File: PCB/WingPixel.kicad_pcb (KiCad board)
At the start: 2 copper layers, 50.8 x 22.9 mm, 21 parts, among them J1 Barrel_Jack, J2 Screw_Terminal_01x04, J3 Conn_01x16, J4 Conn_01x12, J5 TriSolderJumper, J6 Conn_01x02, SW1 SW_Push, U1 WingPixel, U2 LSF0102DCUR

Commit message: Final PCB cleanup, fixed LvlShft wiring.
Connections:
- U2 pad 7: VLED -> Net-(C3-Pad2)
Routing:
- net VLED: track 33.1 -> 28.7 mm
- net Net-(C3-Pad2): track 4.43 -> 4.93 mm
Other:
- board text added: "CLK"
- board text added: "DATA"
- board text added: "GND"
- board text added: "Power Feather From EXT"
- board text added: "VLED"
- board text removed: "EXT >USB"
- board text removed: "LED"

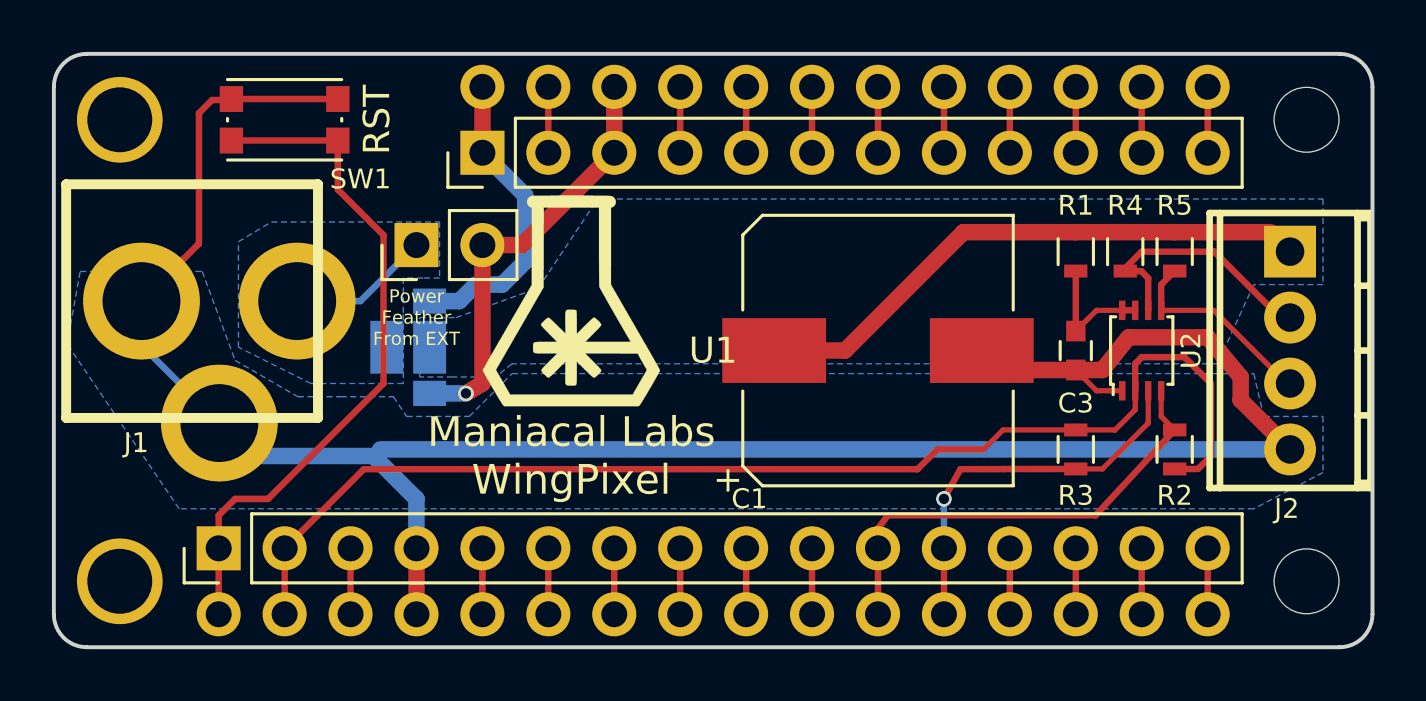
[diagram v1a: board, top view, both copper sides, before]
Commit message: Added placeholders for cuttable traces
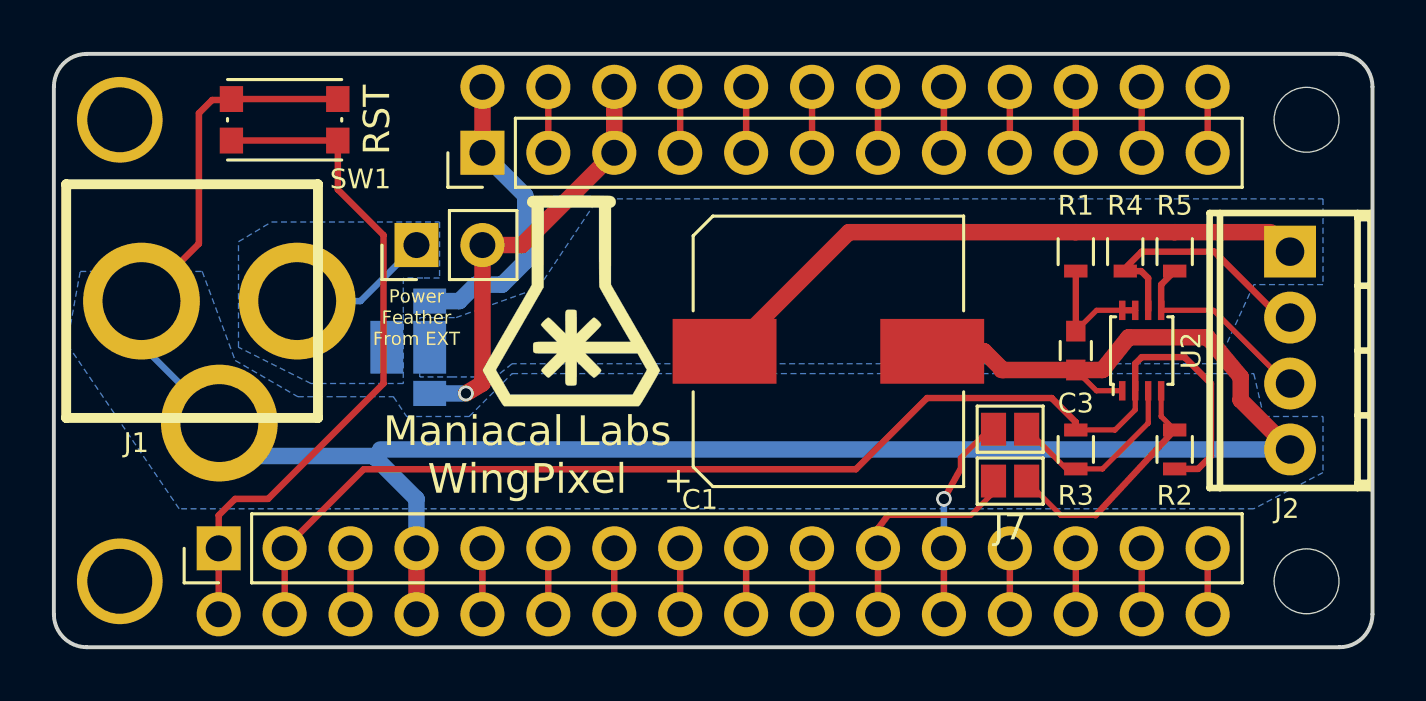
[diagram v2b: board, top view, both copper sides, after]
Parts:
- added J7: GS2, Connectors:GS2, F.Cu at (72.4, 44.4)
- added J8: GS2, Connectors:GS2, F.Cu at (72.4, 42.4)
- moved C1 1.91 mm to (65.4, 39.4)
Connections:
- J3 pad 11: SCLK -> Net-(J3-Pad11)
- J3 pad 12: MOSI -> Net-(J3-Pad12)
- U1 pad 11: SCLK -> Net-(J3-Pad11)
- U1 pad 12: MOSI -> Net-(J3-Pad12)
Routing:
- net Net-(J3-Pad11): track 0.00 -> 8.81 mm
- net SCLK: track 18.2 -> 9.42 mm
- net Net-(J3-Pad12): track 0.00 -> 7.92 mm, vias 0 -> 1
- net MOSI: track 15.0 -> 7.29 mm, vias 1 -> 0
- net GND: track 85.6 -> 87.6 mm
- net VLED: track 28.7 -> 30.7 mm
- net V3v3: track 47.4 -> 48.9 mm

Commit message: Rotated Cap
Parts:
- turned C1 to 270 degrees
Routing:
- net V3v3: track 48.9 -> 15.3 mm
- net VLED: track 30.7 -> 33.7 mm, vias 0 -> 1
- net GND: track 87.6 -> 84.9 mm, vias 0 -> 1
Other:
- board text added: "To Do: Move cap to left, move logo and label to back Fix Cut Trace footprints, re-position."
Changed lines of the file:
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@@
   (general
     (links 64)
-    (no_connects 0)
+    (no_connects 1)
     (area 35.484999 27.864999 86.435001 50.875001)
     (thickness 1.6)
-    (drawings 20)
-    (tracks 144)
+    (drawings 21)
+    (tracks 142)
     (zones 0)
     (modules 23)
@@
   )
   (setup
-    (last_trace_width 0.25)
+    (last_trace_width 0.635)
     (user_trace_width 0.2032)
     (user_trace_width 0.635)
@@
   )
   (module Capacitors_SMD:CP_Elec_10x10 (layer F.Cu)
-    (at 65.4 39.4)
+    (at 65.4 39.4 270)
     (descr "SMT capacitor, aluminium electrolytic, 10x10")
     (attr smd)
-    (fp_text reference C1 (at -4.953 5.715) (layer F.SilkS)
+    (fp_text reference C1 (at -4.953 5.715 270) (layer F.SilkS)
       (effects (font (size 0.762 0.762) (thickness 0.15)))
     )
-    (fp_text value 1000uf (at 0 -6.46) (layer F.Fab)
+    (fp_text value 1000uf (at 0 -6.46 270) (layer F.Fab)
       (effects (font (size 1 1) (thickness 0.15)))
     )
     (fp_circle (center 0 0) (end 0.1 5) (layer F.Fab) (width 0.1))
-    (fp_text user + (at -2.91 -0.08) (layer F.Fab)
-      (effects (font (size 1 1) (thickness 0.15)))
-    )
-    (fp_text user + (at -5.78 4.97) (layer F.SilkS)
-      (effects (font (size 1 1) (thickness 0.15)))
-    )
-    (fp_text user %R (at 0 6.46) (layer F.Fab)
+    (fp_text user + (at -2.91 -0.08 270) (layer F.Fab)
+      (effects (font (size 1 1) (thickness 0.15)))
+    )
+    (fp_text user + (at -5.78 4.97 270) (layer F.SilkS)
+      (effects (font (size 1 1) (thickness 0.15)))
+    )
+    (fp_text user %R (at 0 6.46 270) (layer F.Fab)
       (effects (font (size 1 1) (thickness 0.15)))
     )
@@
     (fp_line (start 6.25 5.3) (end 6.25 -5.31) (layer F.CrtYd) (width 0.05))
     (fp_line (start 6.25 5.3) (end -6.25 5.3) (layer F.CrtYd) (width 0.05))
-    (pad 1 smd rect (at -4 0 180) (size 4 2.5) (layers F.Cu F.Paste F.Mask)
+    (pad 1 smd rect (at -4 0 90) (size 4 2.5) (layers F.Cu F.Paste F.Mask)
       (net 33 VLED))
-    (pad 2 smd rect (at 4 0 180) (size 4 2.5) (layers F.Cu F.Paste F.Mask)
+    (pad 2 smd rect (at 4 0 90) (size 4 2.5) (layers F.Cu F.Paste F.Mask)
       (net 23 GND))
     (model Capacitors_SMD.3dshapes/CP_Elec_10x10.wrl
@@
       (net 35 "Net-(J3-Pad12)"))
   )
+  (gr_text "To Do: Move cap to left, move logo and label to back\nFix Cut Trace footprints, re-position." (at 62.5 53.3) (layer Eco2.User)
+    (effects (font (size 1.5 1.5) (thickness 0.3)))
+  )
   (gr_text GND (at 81.534 43.18) (layer B.SilkS)
     (effects (font (size 1.143 1.143) (thickness 0.2032)) (justify left mirror))
@@
   (segment (start 76.72 37.82) (end 75.73 37.82) (width 0.2032) (layer F.Cu) (net 22))
   (segment (start 75.73 37.82) (end 74.93 38.62) (width 0.2032) (layer F.Cu) (net 22))
-  (segment (start 69.4 39.4) (end 71.4 39.4) (width 0.635) (layer F.Cu) (net 23))
-  (segment (start 71.4 39.4) (end 72.12 40.12) (width 0.635) (layer F.Cu) (net 23))
-  (segment (start 83.185 43.18) (end 48.133 43.18) (width 0.635) (layer B.Cu) (net 23))
+  (segment (start 62.3 43.18) (end 63.28 43.18) (width 0.635) (layer B.Cu) (net 23))
+  (segment (start 63.5 43.4) (end 65.4 43.4) (width 0.635) (layer F.Cu) (net 23) (status 800000))
+  (segment (start 63.3 43.2) (end 63.5 43.4) (width 0.635) (layer F.Cu) (net 23))
+  (via (at 63.3 43.2) (size 0.6) (drill 0.4) (layers F.Cu B.Cu) (net 23))
+  (segment (start 63.28 43.18) (end 63.3 43.2) (width 0.635) (layer B.Cu) (net 23))
+  (segment (start 83.185 43.18) (end 62.3 43.18) (width 0.635) (layer B.Cu) (net 23))
+  (segment (start 62.3 43.18) (end 48.133 43.18) (width 0.635) (layer B.Cu) (net 23))
   (segment (start 48.133 43.18) (end 47.879 43.434) (width 0.25) (layer B.Cu) (net 23))
   (segment (start 49.53 46.99) (end 49.53 45.085) (width 0.635) (layer B.Cu) (net 23))
@@
   (segment (start 76.72 40.92) (end 75.73 40.92) (width 0.2032) (layer F.Cu) (net 23))
   (segment (start 75.73 40.92) (end 74.93 40.12) (width 0.2032) (layer F.Cu) (net 23))
-  (segment (start 74.93 40.12) (end 72.12 40.12) (width 0.635) (layer F.Cu) (net 23))
-  (segment (start 72.12 40.12) (end 72.06 40.12) (width 0.635) (layer F.Cu) (net 23))
-  (segment (start 74.93 42.43) (end 74.93 42.13) (width 0.25) (layer F.Cu) (net 24))
-  (segment (start 47.498 43.942) (end 44.45 46.99) (width 0.25) (layer F.Cu) (net 24))
-  (segment (start 66.458 43.942) (end 47.498 43.942) (width 0.25) (layer F.Cu) (net 24))
-  (segment (start 69.2 41.2) (end 66.458 43.942) (width 0.25) (layer F.Cu) (net 24))
-  (segment (start 74 41.2) (end 69.2 41.2) (width 0.25) (layer F.Cu) (net 24))
-  (segment (start 74.93 42.13) (end 74 41.2) (width 0.25) (layer F.Cu) (net 24))
   (segment (start 74.93 42.43) (end 74.63 42.43) (width 0.2032) (layer F.Cu) (net 24))
   (segment (start 77.22 40.92) (end 77.22 39.874) (width 0.25) (layer F.Cu) (net 24))
@@
   (segment (start 53.594 35.306) (end 57.15 31.75) (width 0.635) (layer F.Cu) (net 32))
   (segment (start 57.15 29.21) (end 57.15 31.75) (width 0.635) (layer F.Cu) (net 32))
-  (segment (start 61.4 39.4) (end 61.6 39.4) (width 0.635) (layer F.Cu) (net 33))
-  (segment (start 61.6 39.4) (end 66.19 34.81) (width 0.635) (layer F.Cu) (net 33))
-  (segment (start 66.19 34.81) (end 70.6 34.81) (width 0.635) (layer F.Cu) (net 33))
+  (segment (start 83.185 35.56) (end 82.76 35.56) (width 0.635) (layer B.Cu) (net 33))
+  (segment (start 82.76 35.56) (end 81.9 34.7) (width 0.635) (layer B.Cu) (net 33))
+  (segment (start 67 35.4) (end 65.4 35.4) (width 0.635) (layer F.Cu) (net 33))
+  (segment (start 67.7 34.7) (end 67 35.4) (width 0.635) (layer F.Cu) (net 33))
+  (via (at 67.7 34.7) (size 0.6) (drill 0.4) (layers F.Cu B.Cu) (net 33))
+  (segment (start 81.9 34.7) (end 67.7 34.7) (width 0.635) (layer B.Cu) (net 33))
   (segment (start 78.74 34.81) (end 76.835 34.81) (width 0.25) (layer F.Cu) (net 33))
   (segment (start 78.74 34.81) (end 82.435 34.81) (width 0.635) (layer F.Cu) (net 33))
   (segment (start 82.435 34.81) (end 83.185 35.56) (width 0.25) (layer F.Cu) (net 33))
-  (segment (start 70.6 34.81) (end 74.93 34.81) (width 0.635) (layer F.Cu) (net 33))
   (segment (start 83.185 35.56) (end 82.804 35.56) (width 0.25) (layer F.Cu) (net 33))
   (segment (start 82.804 35.56) (end 82.054 34.81) (width 0.25) (layer F.Cu) (net 33))

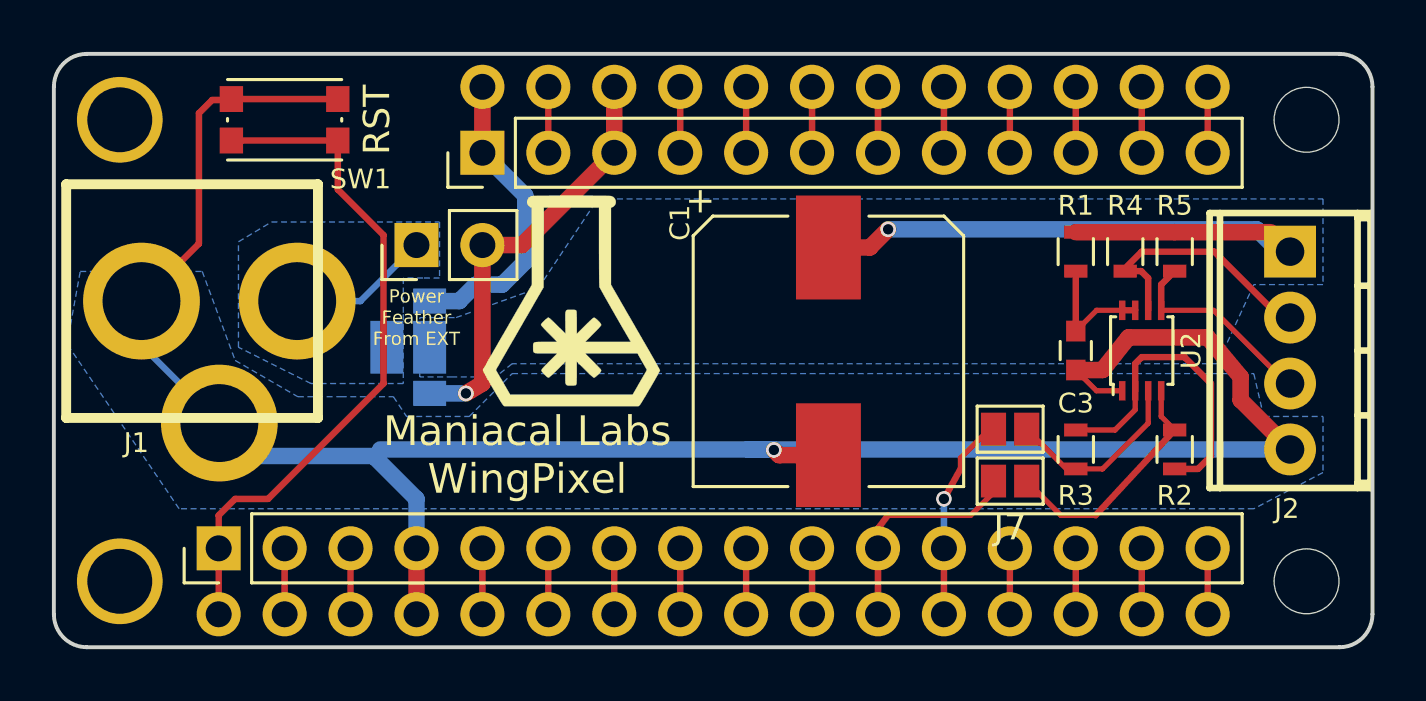
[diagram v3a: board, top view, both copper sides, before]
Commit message: Added Cut Trace footprints, moved cap and logo.
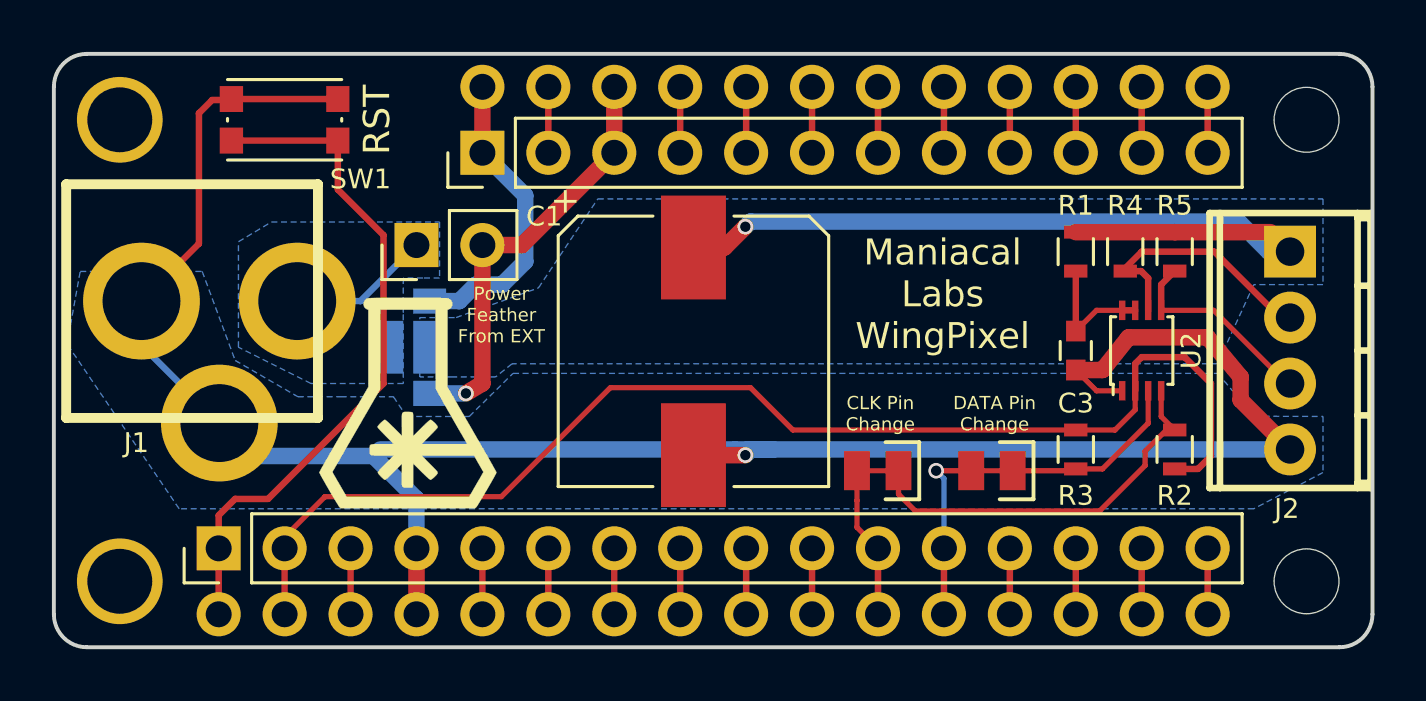
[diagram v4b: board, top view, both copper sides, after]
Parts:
- J7, J8: footprint Connectors:GS2 -> ML_CutTrace:2-PinCutTrace
- moved G*** 7.43 mm to (49.2, 41.4)
- moved J7 5.41 mm to (67.0, 44.0)
- moved C1 5.20 mm to (60.2, 39.4)
- moved J8 1.89 mm to (71.4, 44.0)
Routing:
- net V3v3: track 15.3 -> 49.3 mm
- net VLED: track 33.7 -> 39.5 mm
- net SCLK: track 9.42 -> 15.2 mm
- net Net-(J3-Pad11): track 8.81 -> 5.99 mm
- net Net-(J3-Pad12): track 7.92 -> 7.10 mm
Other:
- board text added: "CLK Pin Change"
- board text added: "DATA Pin Change"
- board text removed: "To Do: Move cap to left, move logo and label to back Fix Cut Trace footprints, re-position."
